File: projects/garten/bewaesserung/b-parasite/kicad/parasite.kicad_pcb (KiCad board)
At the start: 2 copper layers, 22 x 126.4 mm, 31 parts, among them Q1 MMBT3906, Q4 Q_Photo_NPN, SW1 B3U-1000P, U1 E73-2G4M08S1C, U2 SHTC3, Y1 32.768kHz

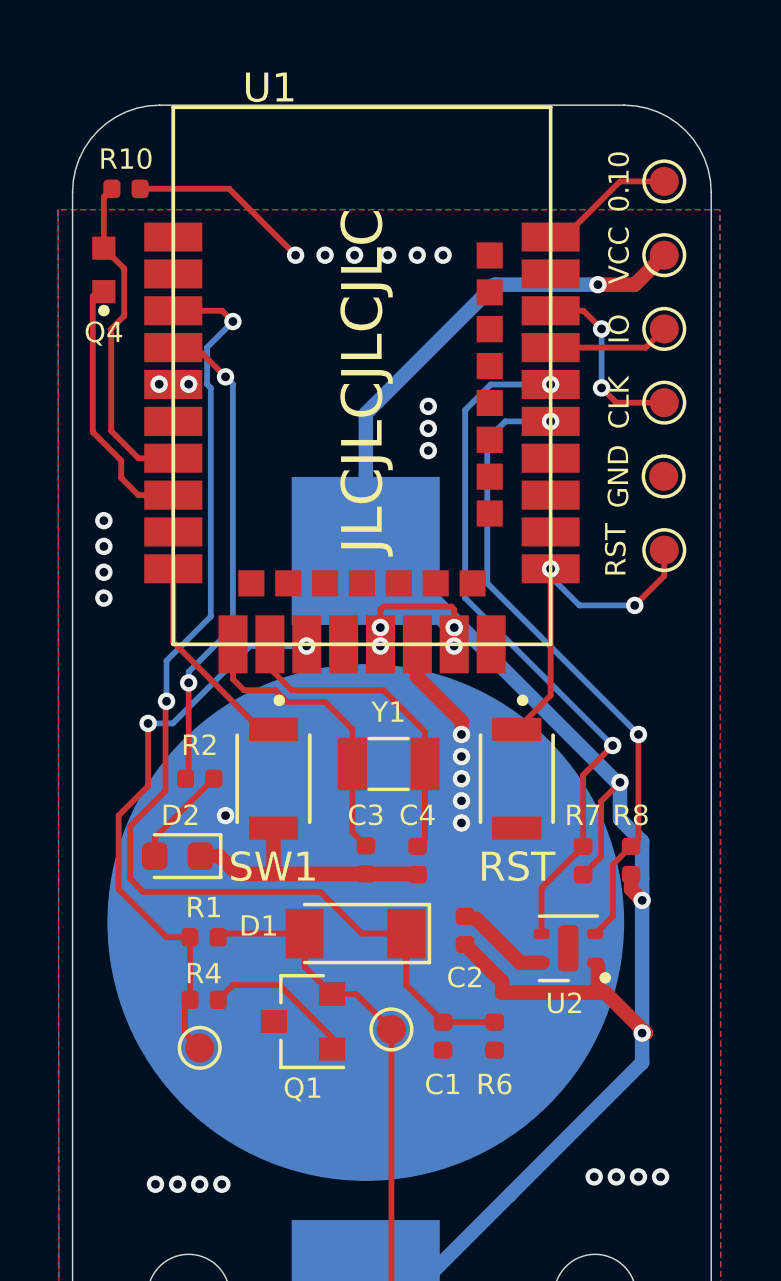
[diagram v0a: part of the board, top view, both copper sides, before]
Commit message: [garten/bewaesserung/b-parasite(pcb)] add mpn to easier order pcb
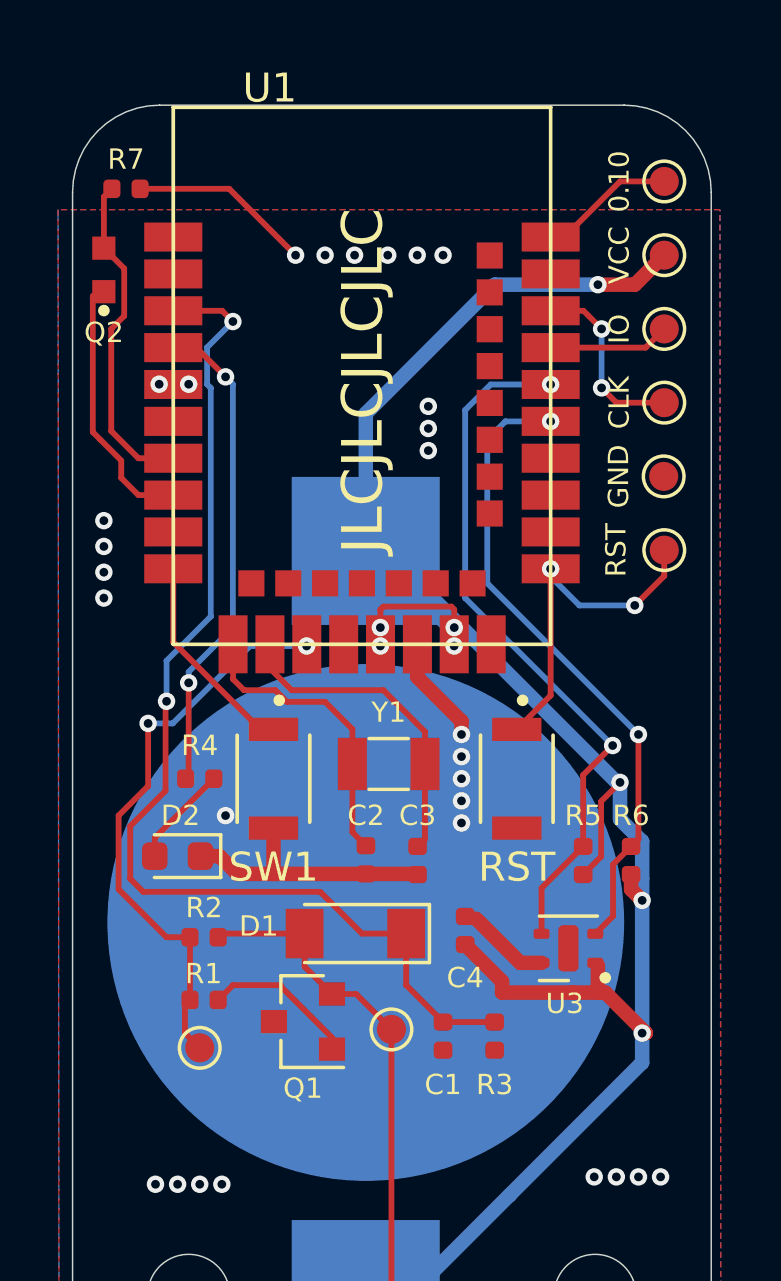
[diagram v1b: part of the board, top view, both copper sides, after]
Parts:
- renumbered C3 to C2, C4 to C3, C2 to C4, Q4 to Q2, R4 to R1, R1 to R2, R6 to R3, R2 to R4, R7 to R5, R8 to R6, R10 to R7, TP8 to TP1, TP7 to TP2, TP1 to TP3, TP2 to TP4, TP3 to TP5, TP4 to TP6, TP5 to TP7, TP6 to TP8, U2 to U3
